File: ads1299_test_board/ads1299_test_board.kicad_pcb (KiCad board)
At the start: 2 copper layers, 61 parts, among them IC1 TPS61023DRLR, IC2 TPS7A2050PDBVR, J1 Conn_01x02, P1 USB_C_Plug_USB2.0, Q1 AO3407A, SW3 SW_SPDT, U1 ADS1299, U2 MCP73832-2-OT, U3 ESP32-S3-WROOM-1, U4 OPA376xxD, U6 AP2112K-3.3, U7 TPD4E05U06DQA

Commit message: PCB design charger and power supply
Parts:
- removed SW3: SW_SPDT, Button_Switch_THT:SW_Slide_SPDT_Straight_CK_OS102011MS2Q
- added R27: 10k, Resistor_SMD:R_0402_1005Metric_Pad0.72x0.64mm_HandSolder, F.Cu at (61.3, 118.8)
- added R28: 10k, Resistor_SMD:R_0402_1005Metric_Pad0.72x0.64mm_HandSolder, F.Cu at (61.3, 120.6)
- added R29: 10k, Resistor_SMD:R_0402_1005Metric_Pad0.72x0.64mm_HandSolder, F.Cu at (61.3, 121.8)
- added R30: 10k, Resistor_SMD:R_0402_1005Metric_Pad0.72x0.64mm_HandSolder, F.Cu at (61.3, 122.9)
- added SW1: EG1218, Button_Switch_THT:SW_Slide-03_Wuerth-WS-SLTV_10x2.5x6.4_P2.54mm, F.Cu at (73.0, 170.1)
- added SW2: SW_MEC_5G, Button_Switch_THT:SW_Push_2P2T_Toggle_CK_PVA2OAH5xxxxxxV2, F.Cu at (26.0, 117.4)
- moved C13 100.2 mm to (61.5, 155.8), turned to 90 degrees
- moved R9 97.2 mm to (64.7, 152.1), turned to 90 degrees
- moved R10 95.2 mm to (66.8, 153.1), turned to 180 degrees
- moved C12 93.7 mm to (68.0, 155.9), turned to 90 degrees
- moved R11 92.8 mm to (69.2, 155.9), turned to -90 degrees
- moved C15 81.0 mm to (75.5, 153.2), turned to -90 degrees
- moved IC1 80.6 mm to (76.2, 155.8)
- moved R14 80.3 mm to (73.0, 153.2), turned to 90 degrees
- moved R16 79.2 mm to (74.2, 153.2), turned to -90 degrees
- moved TP1 72.5 mm to (55.0, 117.8)
- moved C17 70.2 mm to (78.8, 155.7), turned to -90 degrees
- moved C18 68.0 mm to (81.0, 155.7), turned to -90 degrees
- moved IC2 67.9 mm to (86.5, 153.1), turned to 90 degrees
- moved C19 66.0 mm to (83.2, 155.7), turned to -90 degrees
- moved C10 57.2 mm to (169.2, 134.7)
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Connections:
- C12 pad 1: /USB/Vusb_charge -> /USB/Vbus
- C16 pad 1: Vbat -> /USB/Vbus
- D1 pad 2: /USB/Vusb_charge -> /USB/Vbus
- D2 pad 1: Vbat -> Net-(D2-K)
- D2 pad 2: /USB/Vusb_charge -> /USB/Vbus
- IC1 pad 3: Vbat -> /USB/Vbus
- L2 pad 1: Vbat -> /USB/Vbus
- Q1 pad 1: Vbat -> Net-(D2-K)
- Q1 pad 3: Vbat -> /USB/Vbus
- R11 pad 2: /USB/Vusb_charge -> /USB/Vbus
- U1 pad 42: /ESP32_S3_WROOM/GPIO1 -> Net-(U1-GPIO1)
- U1 pad 44: /ESP32_S3_WROOM/GPIO2 -> Net-(U1-GPIO2)
- U1 pad 45: /ESP32_S3_WROOM/GPIO3 -> Net-(U1-GPIO3)
- U1 pad 46: /ESP32_S3_WROOM/GPIO4 -> Net-(U1-GPIO4)
- U2 pad 4: /USB/Vusb_charge -> /USB/Vbus
- U3 pad 12: /ESP32_S3_WROOM/CS -> unconnected-(U3-IO8-Pad12)
- U3 pad 16: /ESP32_S3_WROOM/GPIO2 -> unconnected-(U3-IO46-Pad16)
- U3 pad 17: /ESP32_S3_WROOM/DOUT -> unconnected-(U3-IO9-Pad17)
- U3 pad 18: /ESP32_S3_WROOM/DIN -> /ESP32_S3_WROOM/CS
- U3 pad 19: /ESP32_S3_WROOM/SCLK -> /ESP32_S3_WROOM/DIN
- U3 pad 20: unconnected-(U3-IO12-Pad20) -> /ESP32_S3_WROOM/SCLK
- U3 pad 21: unconnected-(U3-IO13-Pad21) -> /ESP32_S3_WROOM/DOUT
- U3 pad 24: /ESP32_S3_WROOM/GPIO3 -> unconnected-(U3-IO47-Pad24)
- U3 pad 25: /ESP32_S3_WROOM/GPIO4 -> unconnected-(U3-IO48-Pad25)
- U3 pad 26: /ESP32_S3_WROOM/GPIO1 -> unconnected-(U3-IO45-Pad26)
- U3 pad 4: /ESP32_S3_WROOM/Reset_ads1299 -> /ESP32_S3_WROOM/DRDY
- U3 pad 5: /ESP32_S3_WROOM/Power_ads1299 -> /ESP32_S3_WROOM/Reset_ads1299
- U3 pad 7: /ESP32_S3_WROOM/DRDY -> /ESP32_S3_WROOM/Power_ads1299
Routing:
- net VCC: track 0.00 -> 19.7 mm
- net Vbat: track 0.00 -> 15.3 mm
- net /USB/Vbus: track 0.77 -> 11.2 mm
- net Net-(IC1-EN): track 0.00 -> 5.51 mm
- net GND: track 0.77 -> 6.14 mm
- net SW: track 0.00 -> 5.10 mm
- net Net-(D2-K): track 0.00 -> 4.11 mm
- net /ads1299_AFE_/AVDD: track 0.00 -> 3.50 mm
- net /ESP32_S3_WROOM/USB_D-: track 0.77 -> 4.13 mm
- net /ESP32_S3_WROOM/USB_D+: track 0.77 -> 4.13 mm
- net Net-(P1-CC): track 0.00 -> 3.13 mm
- net Net-(U1-GPIO4): track 0.00 -> 2.86 mm
- net Net-(U1-GPIO2): track 0.00 -> 2.86 mm
- net Net-(U2-STAT): track 0.00 -> 2.71 mm
- net Net-(U1-GPIO3): track 0.00 -> 2.59 mm
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- added copper zone on F.Cu, net /USB/Vbus
- added copper zone on F.Cu, net GND
- added copper zone on F.Cu, net Net-(IC1-FB)
- added copper zone on F.Cu, net VCC

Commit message: pcb design
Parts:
- removed C2, C3, C4, C5: 0.15uF, Capacitor_SMD:C_0603_1608Metric_Pad1.08x0.95mm_HandSolder
- removed R1, R2, R3, R4, R5, R6, R7, R8: 10K, Resistor_SMD:R_0402_1005Metric_Pad0.72x0.64mm_HandSolder
- removed SW2: SW_MEC_5G, Button_Switch_THT:SW_Push_2P2T_Toggle_CK_PVA2OAH5xxxxxxV2
- added CN1: W2A45C103MAT2A, W2A45C103MAT2A:W2A45C103MAT2A, F.Cu at (92.5, 113.3)
- added CN2: W2A45C103MAT2A, W2A45C103MAT2A:W2A45C103MAT2A, F.Cu at (92.5, 121.7)
- added J3: Conn_02x05_Top_Bottom, Connector_Molex:Molex_Mini-Fit_Jr_5566-10A_2x05_P4.20mm_Vertical, F.Cu at (114.9, 110.7)
- added R23: CAY16-2201F4LF, CAY16-2201F4LF:RESCAX80P160X320X60-8N, F.Cu at (97.0, 121.7)
- added R31: CAY16-2201F4LF, CAY16-2201F4LF:RESCAX80P160X320X60-8N, F.Cu at (97.0, 113.3)
- moved R12 89.7 mm to (72.0, 130.6)
- moved U3 87.1 mm to (39.6, 85.1)
- moved C28 48.5 mm to (121.7, 146.2)
- moved C10 48.1 mm to (121.7, 142.3)
- moved C9 48.1 mm to (121.7, 140.3)
- moved R20 48.0 mm to (146.9, 135.6)
- moved R21 48.0 mm to (146.9, 137.6)
- moved C7 47.9 mm to (121.7, 136.4)
- moved C6 43.6 mm to (126.3, 135.1)
- moved C1 43.6 mm to (121.7, 134.4)
- moved C21 43.6 mm to (133.5, 134.7)
- moved C22 43.6 mm to (133.0, 136.9)
- moved C24 43.6 mm to (133.0, 138.9)
- moved C8 42.1 mm to (121.7, 138.3)
- moved C11 39.1 mm to (121.7, 144.2)
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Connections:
- U1 pad 18: GND -> unconnected-(U1-SRB2-Pad18)
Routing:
- net /ads1299_AFE_/2P: track 0.00 -> 18.9 mm
- net /ads1299_AFE_/IN2N: track 0.00 -> 18.8 mm
- net /ads1299_AFE_/IN4N: track 0.00 -> 18.8 mm
- net /ads1299_AFE_/4P: track 0.00 -> 18.8 mm
- net /ads1299_AFE_/2N: track 0.00 -> 18.7 mm
- net /ads1299_AFE_/IN4P: track 0.00 -> 18.7 mm
- net /ads1299_AFE_/IN2P: track 0.00 -> 18.7 mm
- net /ads1299_AFE_/3P: track 0.00 -> 18.6 mm
- net /ads1299_AFE_/4N: track 0.00 -> 18.6 mm
- net /ads1299_AFE_/3N: track 0.00 -> 18.5 mm
- net /ads1299_AFE_/1P: track 0.00 -> 18.5 mm
- net /ads1299_AFE_/1N: track 0.00 -> 18.4 mm
- net /ads1299_AFE_/IN1N: track 0.00 -> 18.0 mm
- net /ads1299_AFE_/IN3N: track 0.00 -> 17.9 mm
- net /ads1299_AFE_/IN3P: track 0.00 -> 17.9 mm
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
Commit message: work on PCB
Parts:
- moved R20 131.3 mm to (24.8, 87.4)
- moved R21 131.3 mm to (24.8, 89.4)
- moved C22 121.0 mm to (24.8, 82.6)
- moved C21 121.0 mm to (25.4, 80.4)
- moved R22 82.2 mm to (67.2, 86.6), turned to 180 degrees
- moved J1 76.4 mm to (124.9, 125.5), turned to 0 degrees
- moved J3 69.9 mm to (45.3, 117.2), turned to 90 degrees
- moved C9 62.3 mm to (79.0, 94.9), turned to 180 degrees
- moved R26 61.9 mm to (81.5, 95.7)
- moved U3 61.7 mm to (68.8, 139.4), turned to 180 degrees
- moved C28 60.7 mm to (69.4, 115.3), turned to 90 degrees
- moved R17 60.3 mm to (95.8, 97.2), turned to 180 degrees
- moved C8 60.2 mm to (79.0, 95.9), turned to 180 degrees
- moved R18 54.7 mm to (98.0, 102.2), turned to 0 degrees
- moved C11 54.4 mm to (76.8, 113.5), turned to 90 degrees
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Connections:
- J3 pad 1: /ads1299_AFE_/IN1N -> /ads1299_AFE_/Bias_electrode
- J3 pad 10: /ads1299_AFE_/Bias_electrode -> /ads1299_AFE_/IN4P
- J3 pad 2: /ads1299_AFE_/IN2N -> /ads1299_AFE_/IN1N
- J3 pad 3: /ads1299_AFE_/IN3N -> /ads1299_AFE_/IN2N
- J3 pad 4: /ads1299_AFE_/IN4N -> /ads1299_AFE_/IN3N
- J3 pad 5: /ads1299_AFE_/Ref_electrode -> /ads1299_AFE_/IN4N
- J3 pad 6: /ads1299_AFE_/IN1P -> /ads1299_AFE_/Ref_electrode
- J3 pad 7: /ads1299_AFE_/IN2P -> /ads1299_AFE_/IN1P
- J3 pad 8: /ads1299_AFE_/IN3P -> /ads1299_AFE_/IN2P
- J3 pad 9: /ads1299_AFE_/IN4P -> /ads1299_AFE_/IN3P
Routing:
- net /ESP32_S3_WROOM/Start: track 0.00 -> 45.8 mm, vias 0 -> 2
- net /ESP32_S3_WROOM/Reset_ads1299: track 0.00 -> 40.6 mm, vias 0 -> 2
- net /ESP32_S3_WROOM/Power_ads1299: track 0.00 -> 37.8 mm, vias 0 -> 2
- net /ESP32_S3_WROOM/SCLK: track 0.00 -> 32.1 mm
- net /ESP32_S3_WROOM/DIN: track 0.00 -> 30.9 mm
- net /ESP32_S3_WROOM/CS: track 0.00 -> 30.5 mm, vias 0 -> 2
- net /ESP32_S3_WROOM/USB_D+: track 4.13 -> 23.0 mm
- net /ESP32_S3_WROOM/USB_D-: track 4.13 -> 22.7 mm, vias 0 -> 2
- net /ads1299_AFE_/DVDD: track 0.00 -> 16.2 mm
- net /ads1299_AFE_/AVDD: track 3.50 -> 18.6 mm
- net /ads1299_AFE_/Ref_electrode: track 0.00 -> 11.0 mm
- net /ads1299_AFE_/2N: track 18.7 -> 10.1 mm
- net /ads1299_AFE_/3P: track 18.6 -> 10.1 mm
- net /ads1299_AFE_/2P: track 18.9 -> 10.6 mm
- net /ads1299_AFE_/3N: track 18.5 -> 10.6 mm
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- added copper zone on F.Cu, net /ads1299_AFE_/AVDD
- added copper zone on F.Cu, net GNDD

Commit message: top layer almost finished, bottom layer preview
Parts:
- moved R20 76.2 mm to (82.2, 137.5), turned to 180 degrees
- moved C22 66.9 mm to (89.8, 98.8), turned to 90 degrees
- moved C21 65.2 mm to (88.1, 98.3), turned to 90 degrees
- moved R21 47.7 mm to (58.1, 123.5)
- moved J1 28.7 mm to (104.7, 105.1), turned to -90 degrees
- moved U3 4.87 mm to (70.4, 134.8)
- moved R24 1.58 mm to (94.2, 139.7), turned to -90 degrees
- moved R17 0.20 mm to (95.8, 97.0)
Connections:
- C21 pad 1: /ESP32_S3_WROOM/3.3V -> /ads1299_AFE_/DVDD
- C22 pad 1: /ESP32_S3_WROOM/3.3V -> /ads1299_AFE_/DVDD
- R20 pad 1: /ESP32_S3_WROOM/3.3V -> /ads1299_AFE_/DVDD
- R21 pad 1: /ESP32_S3_WROOM/3.3V -> /ads1299_AFE_/DVDD
- U3 pad 2: /ESP32_S3_WROOM/3.3V -> /ads1299_AFE_/DVDD
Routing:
- net GND: track 8.89 -> 188.5 mm, vias 0 -> 61
- net /ads1299_AFE_/DVDD: track 16.2 -> 94.5 mm, vias 0 -> 2
- net GNDD: track 2.27 -> 69.5 mm, vias 1 -> 35
- net /ESP32_S3_WROOM/DRDY: track 0.00 -> 48.4 mm, vias 0 -> 2
- net /ESP32_S3_WROOM/DOUT: track 5.30 -> 26.6 mm, vias 0 -> 2
- net /ads1299_AFE_/SRB1: track 5.48 -> 26.6 mm
- net /USB/Vbus: track 11.2 -> 28.9 mm
- net Net-(SW1-A): track 0.00 -> 15.3 mm
- net /ads1299_AFE_/AVDD: track 18.6 -> 32.6 mm
- net /ESP32_S3_WROOM/Reset_ads1299: track 40.6 -> 35.0 mm, vias 2 -> 0
- net /ESP32_S3_WROOM/Start: track 45.8 -> 40.5 mm
- net /ESP32_S3_WROOM/Power_ads1299: track 37.8 -> 32.6 mm, vias 2 -> 0
- net /ESP32_S3_WROOM/CS: track 30.5 -> 26.9 mm
- net /ESP32_S3_WROOM/DIN: track 30.9 -> 27.7 mm
- net /ESP32_S3_WROOM/SCLK: track 32.1 -> 29.1 mm
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
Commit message: final form
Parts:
- added C26: 15nF, Capacitor_SMD:C_0402_1005Metric_Pad0.74x0.62mm_HandSolder, F.Cu at (140.4, 73.9)
- added R25: 1M, Resistor_SMD:R_0402_1005Metric_Pad0.72x0.64mm_HandSolder, F.Cu at (140.4, 72.9)
- TP1: footprint TestPoint:TestPoint_Pad_D1.5mm -> TestPoint:TestPoint_Pad_D1.0mm
- moved C1 68.2 mm to (142.2, 91.1)
- moved C10 68.2 mm to (143.2, 91.1)
- moved C11 68.2 mm to (141.2, 91.1)
- moved C13 68.2 mm to (161.8, 105.8)
- moved C16 68.2 mm to (162.6, 93.6)
- moved C21 68.2 mm to (152.5, 75.9)
- moved C28 68.2 mm to (133.8, 93.0)
- moved C7 68.2 mm to (146.7, 91.1)
- moved C8 68.2 mm to (143.4, 73.5)
- moved C9 68.2 mm to (143.4, 72.5)
- moved CN1 68.2 mm to (133.0, 85.7)
- moved CN2 68.2 mm to (133.0, 81.8)
- moved D1 68.2 mm to (157.6, 100.1)
- moved D2 68.2 mm to (166.0, 102.5)
- moved IC1 68.2 mm to (161.8, 91.1)
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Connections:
- C24 pad 1: /ESP32_S3_WROOM/en -> /ads1299_AFE_/DVDD
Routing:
- net GND: track 188.5 -> 22.8 mm, vias 61 -> 60
- net GNDD: track 69.5 -> 9.38 mm, vias 35 -> 32
- net /ads1299_AFE_/Bias_out: track 0.00 -> 46.6 mm, vias 0 -> 2
- net /ads1299_AFE_/AVDD: track 32.6 -> 74.5 mm
- net /USB/Vbus: track 28.9 -> 41.4 mm
- net /ads1299_AFE_/Bias_electrode: track 0.00 -> 8.25 mm
- net Net-(U1-BIASREF): track 0.00 -> 8.06 mm
- net /ads1299_AFE_/DVDD: track 94.5 -> 102.2 mm, vias 2 -> 4
- net Net-(U1-BIASINV): track 0.00 -> 3.66 mm
- net /ESP32_S3_WROOM/DRDY: track 48.4 -> 50.0 mm
- net /ESP32_S3_WROOM/Power_ads1299: track 32.6 -> 31.5 mm
- added copper zone on B.Cu, net GND
- added copper zone on B.Cu, net GNDD
- removed copper zone on F.Cu, net /ads1299_AFE_/AVDD
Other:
- board outline added: 65.4 x 54.6 mm

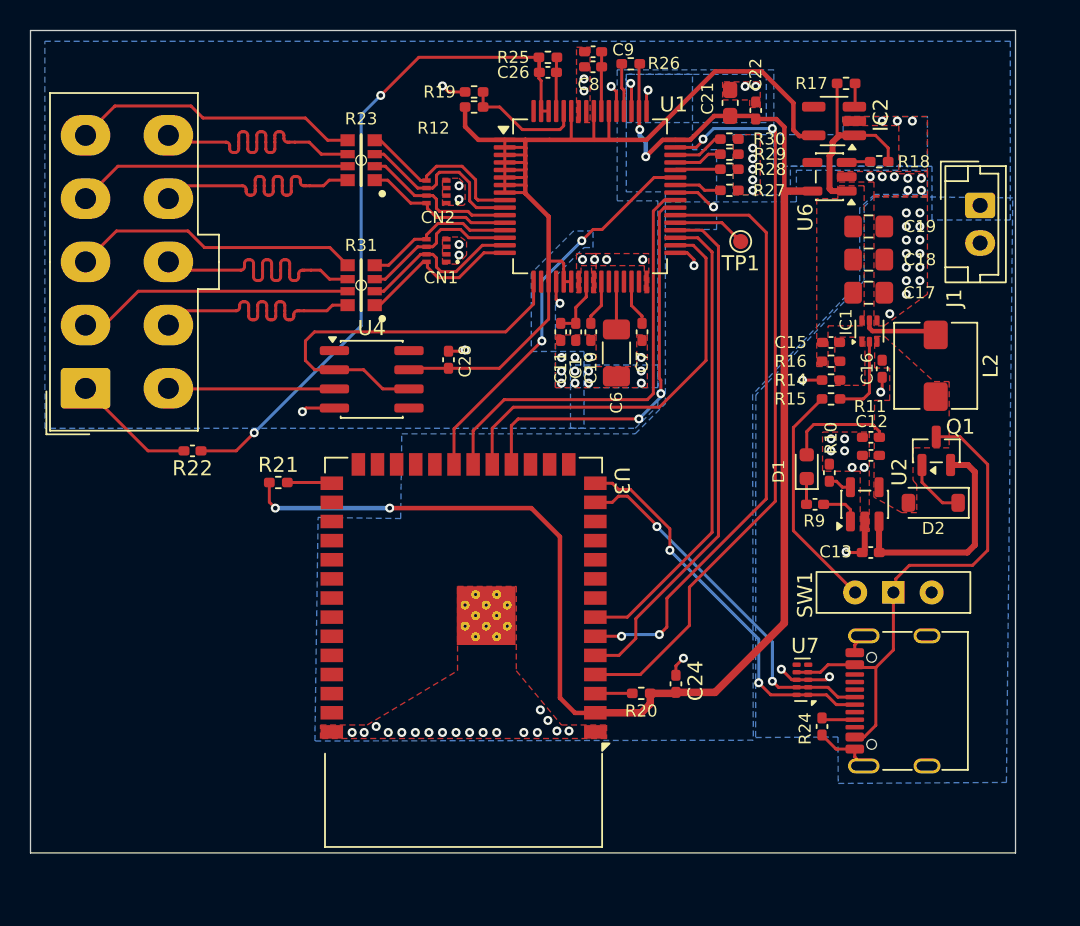
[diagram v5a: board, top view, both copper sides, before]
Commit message: fuse and 1ohm r
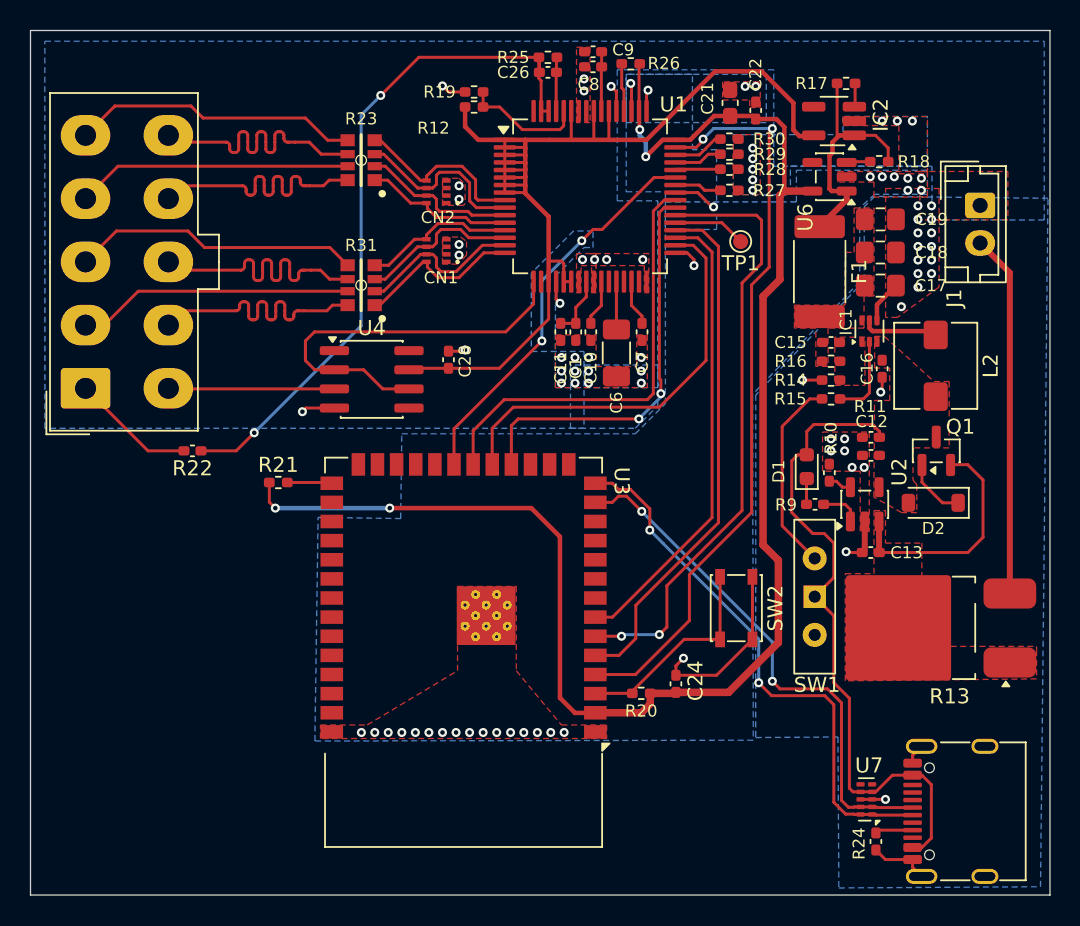
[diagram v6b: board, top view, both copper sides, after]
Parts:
- added F1: Fuse_Small, Fuse:Fuse_2512_6332Metric_Pad1.52x3.35mm_HandSolder, F.Cu at (158.4, 87.1)
- added R13: 1ohm, Package_TO_SOT_SMD:TO-252-2_TabPin1, F.Cu at (165.7, 110.8)
- added SW2: PTS810SJM250SMTR LFS, Button_Switch_SMD:SW_SPST_PTS810, F.Cu at (152.9, 109.5)
- moved U7 9.00 mm to (161.5, 122.2)
- moved R24 8.43 mm to (162.2, 125.0)
- moved P1 8.28 mm to (168.3, 123.0)
- moved SW1 5.23 mm to (158.1, 108.7), turned to -90 degrees
- moved C17 0.91 mm to (162.5, 88.1)
- moved C18 0.91 mm to (162.5, 85.9)
- moved C19 0.91 mm to (162.5, 83.7)
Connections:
- C15 pad 1: VCC -> Net-(IC1-VOUT)
- C17 pad 1: VCC -> Net-(IC1-VOUT)
- C18 pad 1: VCC -> Net-(IC1-VOUT)
- C19 pad 1: VCC -> Net-(IC1-VOUT)
- C21 pad 2: GNDD -> GND
- C22 pad 2: GNDD -> GND
- C24 pad 2: GNDD -> GND
- IC1 pad 6: VCC -> Net-(IC1-VOUT)
- R15 pad 1: Net-(SW1-A) -> Net-(SW1-C)
- R16 pad 1: VCC -> Net-(IC1-VOUT)
- SW1 pad 2: unconnected-(SW1-C-Pad2) -> Net-(SW1-C)
- SW1 pad 3: Net-(SW1-A) -> unconnected-(SW1-A-Pad3)
- U1 pad 33: GNDD -> GND
- U1 pad 41: GNDD -> GND
- U1 pad 49: GNDD -> GND
- U1 pad 51: GNDD -> GND
- U3 pad 1: GNDD -> GND
- U3 pad 40: GNDD -> GND
- U3 pad 41: GNDD -> GND
- U6 pad 2: GNDD -> GND
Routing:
- net Net-(J1-Pin_2): track 0.00 -> 24.1 mm
- net GND: track 22.8 -> 43.4 mm, vias 60 -> 89
- net Net-(SW1-A): track 15.3 -> 0.00 mm
- net Net-(SW1-C): track 0.00 -> 13.1 mm
- net /ESP32_S3_WROOM/en: track 2.46 -> 14.0 mm
- net /ESP32_S3_WROOM/USB_D+: track 25.8 -> 36.5 mm
- net /ESP32_S3_WROOM/USB_D-: track 24.5 -> 35.1 mm
- net GNDD: track 9.38 -> 0.00 mm, vias 32 -> 0
- net VCC: track 13.1 -> 16.2 mm
- net /USB/Vbus: track 41.4 -> 44.4 mm
- net /ads1299_AFE_/DVDD: track 102.2 -> 103.6 mm
- net /ESP32_S3_WROOM/Power_ads1299: track 31.5 -> 30.9 mm
- added copper zone on B.Cu, net (none)
- added copper zone on F.Cu, net (none)
- added copper zone on F.Cu, net Net-(IC1-VOUT)
- added copper zone on F.Cu, net Vbat
- removed copper zone on B.Cu, net GNDD
- removed copper zone on F.Cu, net GNDD
- removed copper zone on F.Cu, net VCC
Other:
- board size 65.4 x 54.6 mm -> 67.7 x 57.4 mm

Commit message: 8 channel
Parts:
- removed J3: Conn_02x05_Top_Bottom, Connector_Molex:Molex_Mini-Fit_Jr_5566-10A_2x05_P4.20mm_Vertical
- added CN3: W2A45C103MAT2A, W2A45C103MAT2A:W2A45C103MAT2A, B.Cu at (136.6, 81.2)
- added CN4: W2A45C103MAT2A, W2A45C103MAT2A:W2A45C103MAT2A, B.Cu at (136.6, 78.9)
- added J2: Conn_02x10_Counter_Clockwise, Connector_IDC:IDC-Header_2x10_P2.54mm_Vertical, F.Cu at (117.3, 99.9)
- added R32: CAY16-2201F4LF, CAY16-2201F4LF:RESCAX80P160X320X60-8N, F.Cu at (126.4, 79.0)
- added R33: CAY16-2201F4LF, CAY16-2201F4LF:RESCAX80P160X320X60-8N, F.Cu at (126.4, 83.0)
- CN1, CN2: moved to B.Cu
- moved R22 32.8 mm to (136.2, 72.6)
- moved R23 7.44 mm to (126.4, 87.0)
- moved R19 6.13 mm to (141.0, 72.5), turned to 0 degrees
- moved R12 6.10 mm to (141.0, 73.6), turned to 180 degrees
- moved CN2 3.97 mm to (136.6, 83.5), turned to -90 degrees
- moved CN1 3.60 mm to (136.6, 85.8), turned to -90 degrees
- moved R31 3.42 mm to (126.4, 91.0)
- moved U4 2.21 mm to (130.3, 95.8)
- moved C26 1.73 mm to (138.7, 73.6)
- moved R25 1.73 mm to (138.7, 72.6)
- moved C28 0.99 mm to (134.7, 93.4)
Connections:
- CN1 pad 5: /ads1299_AFE_/2N -> /ads1299_AFE_/1P
- CN1 pad 6: /ads1299_AFE_/2P -> /ads1299_AFE_/1N
- CN1 pad 7: /ads1299_AFE_/1N -> /ads1299_AFE_/2P
- CN1 pad 8: /ads1299_AFE_/1P -> /ads1299_AFE_/2N
- CN2 pad 5: /ads1299_AFE_/4N -> /ads1299_AFE_/3P
- CN2 pad 6: /ads1299_AFE_/4P -> /ads1299_AFE_/3N
- CN2 pad 7: /ads1299_AFE_/3N -> /ads1299_AFE_/4P
- CN2 pad 8: /ads1299_AFE_/3P -> /ads1299_AFE_/4N
- U1 pad 1: /ads1299_AFE_/AVDD -> /ads1299_AFE_/8N
- U1 pad 2: /ads1299_AFE_/AVDD -> /ads1299_AFE_/8P
- U1 pad 3: /ads1299_AFE_/AVDD -> /ads1299_AFE_/7N
- U1 pad 4: /ads1299_AFE_/AVDD -> /ads1299_AFE_/7P
- U1 pad 5: /ads1299_AFE_/AVDD -> /ads1299_AFE_/6N
- U1 pad 6: /ads1299_AFE_/AVDD -> /ads1299_AFE_/6P
- U1 pad 7: /ads1299_AFE_/AVDD -> /ads1299_AFE_/5N
- U1 pad 8: /ads1299_AFE_/AVDD -> /ads1299_AFE_/5P
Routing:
- net /ads1299_AFE_/Bias_out: track 46.6 -> 5.97 mm, vias 2 -> 0
- net /ads1299_AFE_/AVDD: track 74.5 -> 99.9 mm
- net /ads1299_AFE_/Ref_electrode: track 11.0 -> 31.4 mm
- net /ads1299_AFE_/Bias_electrode: track 8.25 -> 23.7 mm
- net /ads1299_AFE_/8N: track 0.00 -> 14.5 mm, vias 0 -> 1
- net /ads1299_AFE_/6P: track 0.00 -> 14.3 mm, vias 0 -> 1
- net /ads1299_AFE_/8P: track 0.00 -> 14.0 mm, vias 0 -> 1
- net /ads1299_AFE_/7P: track 0.00 -> 13.7 mm, vias 0 -> 1
- net /ads1299_AFE_/7N: track 0.00 -> 13.7 mm, vias 0 -> 1
- net /ads1299_AFE_/6N: track 0.00 -> 13.5 mm, vias 0 -> 1
- net /ads1299_AFE_/IN5N: track 0.00 -> 13.4 mm
- net /ads1299_AFE_/5N: track 0.00 -> 13.1 mm, vias 0 -> 1
- net /ads1299_AFE_/IN6N: track 0.00 -> 13.0 mm
- net /ads1299_AFE_/5P: track 0.00 -> 13.0 mm, vias 0 -> 1
- net /ads1299_AFE_/IN7N: track 0.00 -> 12.9 mm
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- removed copper zone on B.Cu, net (none)
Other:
- board size 67.7 x 57.4 mm -> 67.9 x 57.6 mm
